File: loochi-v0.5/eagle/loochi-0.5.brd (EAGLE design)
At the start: 67.8 x 63.5 mm, 49 parts, among them IC1 ATTINY61M, J1 SPI_PRG, J2 POWER_JACKSMD, Q1 PMN25ENSOT457, Q2 PMN25ENSOT457, Q3 PMN25ENSOT457, Q4 FDC654P, U1 LZ4-00MC00BIGPADS, U2 APDS-9007, X1 SMA-SMD

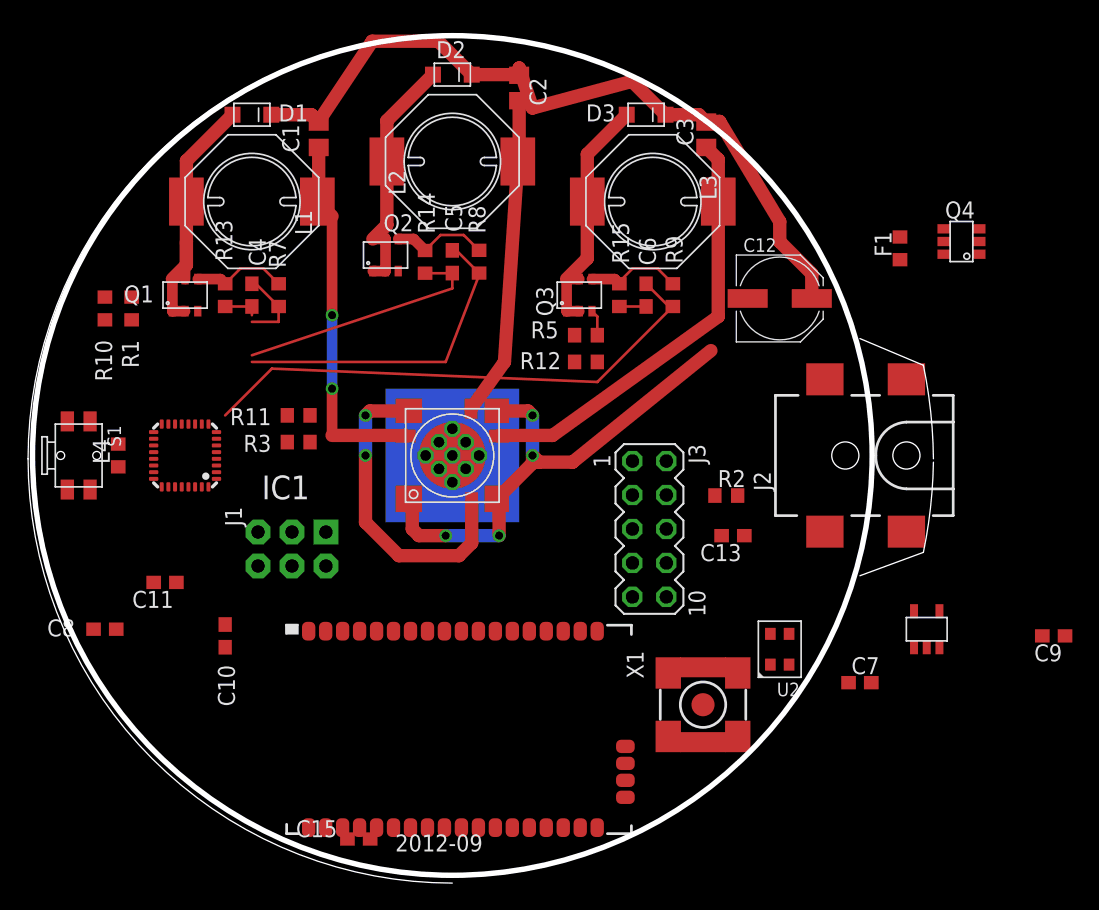
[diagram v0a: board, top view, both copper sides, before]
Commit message: Finalized board layout but have not run DRC yet.
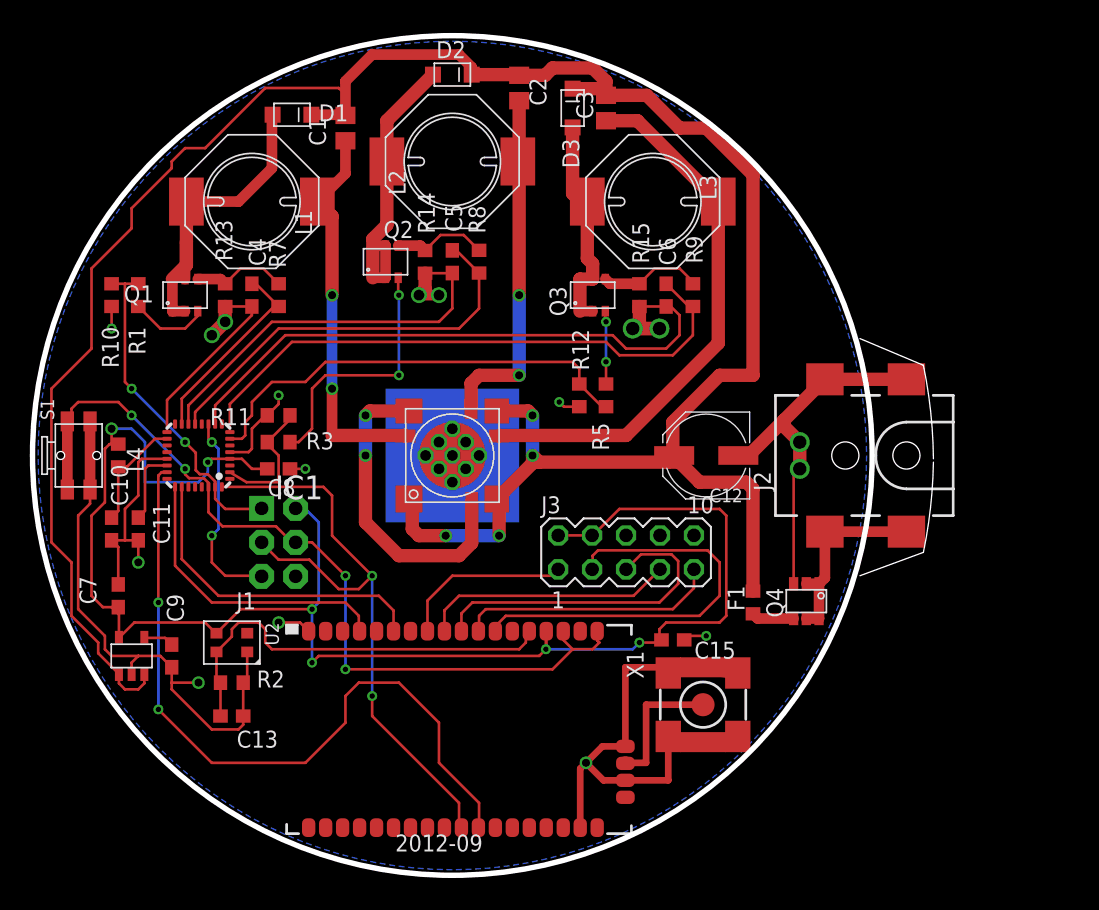
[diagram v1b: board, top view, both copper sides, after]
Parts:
- moved C9 66.0 mm to (11.0, 17.0), turned to 270 degrees
- moved U$1 59.5 mm to (8.00, 17.0)
- moved C7 55.9 mm to (7.00, 21.5), turned to 90 degrees
- moved U2 41.0 mm to (15.5, 18.0), turned to 180 degrees
- moved C13 39.9 mm to (15.5, 12.5), turned to 0 degrees
- moved R2 39.6 mm to (15.5, 15.0), turned to 180 degrees
- moved Q4 29.3 mm to (58.5, 21.1), turned to 180 degrees
- moved F1 28.7 mm to (54.5, 21.0)
- moved C15 27.8 mm to (48.5, 18.2), turned to 180 degrees
- moved C8 17.7 mm to (19.0, 31.0)
- moved C12 13.0 mm to (51.0, 32.0), turned to 180 degrees
- moved C10 11.7 mm to (6.50, 26.5)
- moved C3 7.76 mm to (43.5, 58.0)
- moved D3 5.52 mm to (41.0, 58.0), turned to 90 degrees
- moved R5 4.74 mm to (43.5, 36.5), turned to 90 degrees
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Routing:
- net GND: track 23.7 -> 248.0 mm, vias 0 -> 17
- net VCC: track 0.00 -> 120.7 mm, vias 0 -> 6
- net V+: track 96.4 -> 182.1 mm
- net BUTTON/MOSI: track 0.00 -> 63.3 mm, vias 0 -> 4
- net BLE-SCK: track 0.00 -> 54.9 mm, vias 0 -> 2
- net BLE-CS/SCK: track 0.00 -> 47.5 mm, vias 0 -> 2
- net BPWM: track 0.00 -> 33.8 mm
- net AIO0: track 0.00 -> 31.9 mm
- net N$15: track 0.00 -> 31.7 mm
- net RPWM/MISO: track 0.00 -> 25.1 mm, vias 0 -> 2
- net RSTB: track 0.00 -> 24.7 mm
- net BLE-MOSI: track 0.00 -> 24.4 mm
- net BLE-MISO: track 0.00 -> 22.4 mm
- net SPI_MISO: track 0.00 -> 19.5 mm
- net N$4: track 0.00 -> 19.3 mm, vias 0 -> 2
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- added copper zone on layer 16, net GND
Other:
- board size 67.8 x 63.5 mm -> 67.4 x 62.8 mm
- board text removed: "CC-BY-SA"
- board text removed: "Open-Source Hardware"

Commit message: Continued work on board v0.5 - Integrated Jurgen v0.5.1 changes - Shielded bsense - Holes for lenses - drc ok now
Next steps: BOM & check parts footprint
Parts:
- removed F1: MPZ2012, rcl:R0603
- removed J3: (no value), con-lstb:MA05-2
- added BLUE: (no value), WCI:CHIPLED_0603
- added C14, C16: 100n, rcl:C0603
- added C19: 0.1uF, rcl:C0603K
- added F2: MPZ2012, rcl:R0603
- added P1: 53047-0610, con-molex-picoblade:53047-0610
- added R18: 2, rcl:R0603
- added R4: 1k, rcl:R0603
- C7: value 10uF X5R Low ESR -> 10u
- Q4: value FDC654P -> SI7617DN; device mosfet:SUPERSOT6 -> Oma:POWERPAK1212-8
- moved C15 8.81 mm to (40.0, 20.5)
- moved X1 3.39 mm to (53.1, 15.8), turned to 135 degrees
- moved Q4 3.13 mm to (56.0, 23.0), turned to 0 degrees
- moved C7 1.12 mm to (6.50, 22.5)
- moved C13 0.50 mm to (15.5, 13.0)
- moved C8 0.50 mm to (19.0, 31.5)
- moved L4 0.50 mm to (7.50, 32.0)
- moved R11 0.50 mm to (19.0, 34.5)
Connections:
- removed net N$6: F1.1, Q4.P$4
- removed net RSTB: J3.5, U$2.CSB
- new net N$12: BLUE.C, R4.2
- new net N$16: R4.1, U$2.LED(1)
- new net N$21: C12.+, R18.1
- new net N$22: C19.2, F2.2, U$1.1, U$1.3
- new net SPI_CSB: P1.3, U$2.CSB
- new net SPI_RESET: P1.1, U$2.RESET
- net GND: now also C16.2, C19.1, P1.6, Q4.P$4; no longer J3.10, J3.6, J3.8, Q4.P$3
- net N$10: now also Q4.P$7, Q4.P$8; no longer Q4.P$1, Q4.P$2
- net N$15: now also C14.2, C16.1, X1.1; no longer J3.3, U$2.RESET
- net N$2: now also C14.1; no longer X1.1
- net SPI_CLK: now also P1.4; no longer J3.7
- net SPI_MISO: now also P1.5; no longer J3.9
- net SPI_MOSI: now also P1.2; no longer J3.1
- net V+: now also F2.1, Q4.P$1, Q4.P$2, Q4.P$3, R18.2; no longer C12.+, F1.2, U$1.1, U$1.3
- net VCC: now also BLUE.A; no longer J3.2, J3.4
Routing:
- net GND: track 248.0 -> 316.8 mm, vias 17 -> 18
- net VCC: track 120.7 -> 90.6 mm, vias 6 -> 4
- net N$16: track 0.00 -> 26.0 mm
- net RSTB: track 24.7 -> 0.00 mm
- net N$15: track 31.7 -> 9.29 mm
- net SPI_CSB: track 0.00 -> 20.2 mm
- net SPI_RESET: track 0.00 -> 19.9 mm
- net V+: track 182.1 -> 162.7 mm
- net N$22: track 0.00 -> 16.4 mm
- net SPI_MOSI: track 13.0 -> 25.7 mm
- net BLE-SCK: track 54.9 -> 42.9 mm
- net N$2: track 10.2 -> 3.65 mm
- net N$21: track 0.00 -> 5.28 mm
- net SPI_MISO: track 19.5 -> 15.2 mm, vias 0 -> 1
- net N$10: track 14.7 -> 11.5 mm
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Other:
- board size 67.4 x 62.8 mm -> 67.8 x 63.5 mm

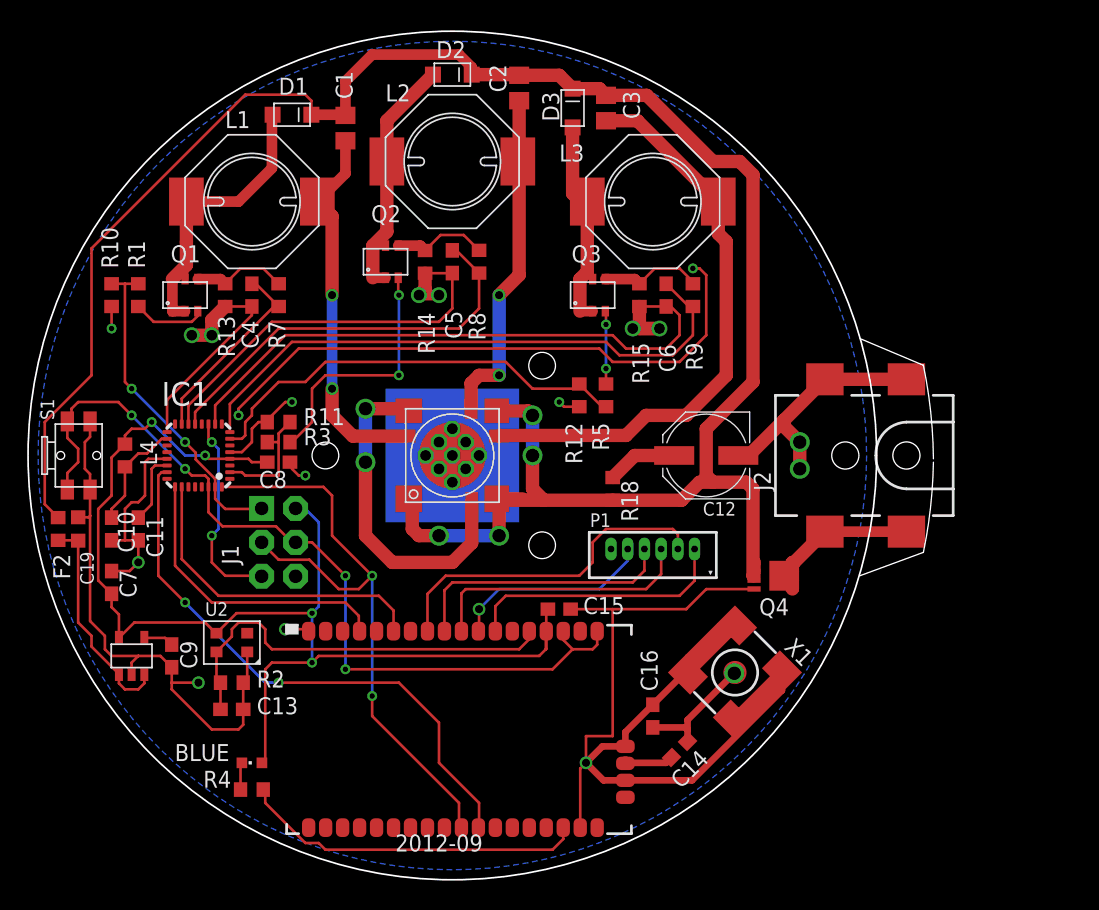
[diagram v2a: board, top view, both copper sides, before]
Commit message: More work on the board - almost final (antenna trace needs rework)
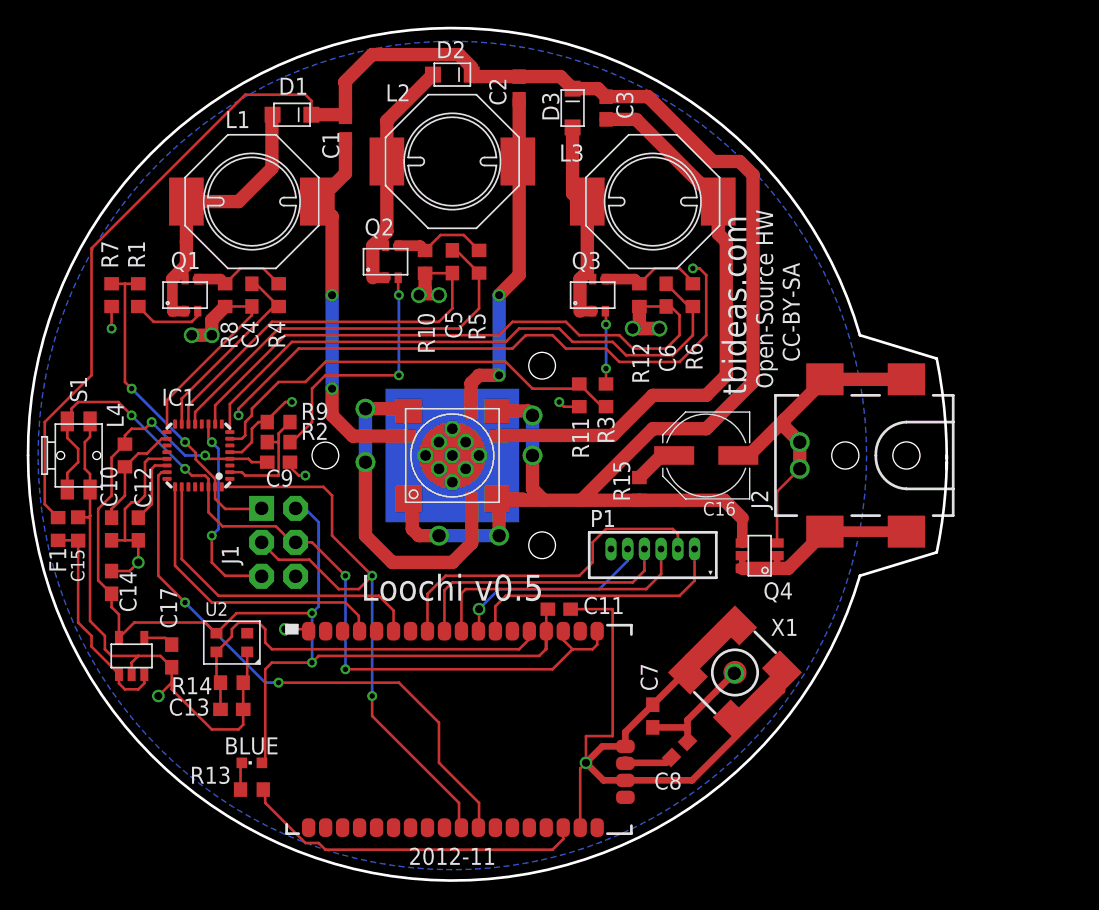
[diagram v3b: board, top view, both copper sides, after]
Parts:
- removed C19: 0.1uF, rcl:C0603K
- removed R18: 2, rcl:R0603
- added C17: 10nF, rcl:C0603
- added R6: 10k, rcl:R0603
- C1, C2, C3: device rcl:C0805 -> rcl:C0603
- C11, C8: value 0.1uF -> 100n
- C12: value 100uF -> 0.1uF; device rcl:PANASONIC_D -> rcl:C0603
- C14: value 100n -> 10u
- C15: value 100n -> 0.1uF; device rcl:C0603 -> rcl:C0603K
- C16: value 100n -> 100uF; device rcl:C0603 -> rcl:PANASONIC_D
- C7: value 10u -> 100n
- C9: value 10nF -> 0.1uF
- Q4: value SI7617DN -> (none); device Oma:POWERPAK1212-8 -> mosfet:SUPERSOT6
- R10, R12, R8: value 10k -> 0.1
- R13: value 0.1 -> 1k
- R14: value 0.1 -> 27k
- R15: value 0.1 -> 2
- R2: value 27k -> 10
- R4: value 1k -> 10k
- R5: value 10 -> 10k
- U$1: value LP2985 -> AIRCABLEBLPEXTANT; device ti-regulators:DBV -> aircable:AIRCABLEBLP
- U$2: value AIRCABLEBLPEXTANT -> LP2985; device aircable:AIRCABLEBLP -> ti-regulators:DBV
- moved C14 44.3 mm to (6.50, 22.5), turned to 90 degrees
- moved C12 42.9 mm to (8.50, 26.5), turned to 90 degrees
- moved C7 41.7 mm to (47.0, 12.5)
- moved R13 37.1 mm to (17.0, 7.00), turned to 180 degrees
- moved R4 37.1 mm to (19.0, 44.0), turned to 90 degrees
- moved C8 36.9 mm to (49.0, 10.0), turned to 45 degrees
- moved C15 36.5 mm to (4.00, 26.5), turned to 270 degrees
- moved R14 34.7 mm to (15.5, 15.0), turned to 180 degrees
- moved R9 32.4 mm to (19.0, 34.5), turned to 0 degrees
- moved C11 32.1 mm to (40.0, 20.5), turned to 180 degrees
- moved U$1 25.1 mm to (32.5, 11.5)
- moved U$2 25.1 mm to (8.00, 17.0)
- moved R3 24.7 mm to (43.5, 36.5), turned to 90 degrees
- moved R10 23.6 mm to (30.0, 46.5)
- moved R11 22.6 mm to (41.5, 36.5), turned to 90 degrees
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- renumbered F2 to F1
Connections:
- net AIO0: now also R14.2, U$1.AIO(0); no longer R2.2, U$2.AIO(0)
- net BLE-CS/SCK: now also U$1.PIO(4); no longer U$2.PIO(4)
- net BLE-MISO: now also U$1.RX; no longer U$2.RX
- net BLE-MOSI: now also U$1.TX; no longer U$2.TX
- net BLE-SCK: now also U$1.PIO(3); no longer U$2.PIO(3)
- net BPWM: now also R11.2, R3.1; no longer R12.2, R5.1
- net BSENSE: now also R6.1; no longer R9.1
- net BUTTON/MOSI: now also U$1.PIO(10), U$1.VREG_EN; no longer U$2.PIO(10), U$2.VREG_EN
- net GND: now also C12.1, C14.2, C16.-, C17.2, C9.1, Q4.P$3, R7.1, R8.1, R9.1, U$1.GND4, U$1.GND5, U$1.GND@28, U$1.GND@58, U$2.2; no longer C12.-, C16.2, C19.1, C8.1, C9.2, Q4.P$4, R13.1, R15.1, R2.1, U$1.2, U$2.GND4, U$2.GND5, U$2.GND@28, U$2.GND@58
- net GPWM: now also R2.1, R9.2; no longer R11.2, R3.1
- net GSENSE: now also R5.1; no longer R8.1
- net N$10: now also Q4.P$1, Q4.P$2; no longer Q4.P$7, Q4.P$8
- net N$12: now also R13.2; no longer R4.2
- net N$13: now also C17.1, U$2.4; no longer C9.1, U$1.4
- net N$15: now also C7.1, C8.2; no longer C14.2, C16.1
- net N$16: now also R13.1, U$1.LED(1); no longer R4.1, U$2.LED(1)
- net N$17: now also R10.2, R5.2; no longer R14.2, R8.2
- net N$2: now also C8.1, U$1.ANT; no longer C14.1, U$2.ANT
- net N$21: now also C16.+, R15.1; no longer C12.+, R18.1
- net N$22: now also C15.2, U$2.1, U$2.3; no longer C19.2, U$1.1, U$1.3
- net N$25: now also R12.2, R6.2; no longer R15.2, R9.2
- net N$3: now also R3.2; no longer R5.2
- net N$4: now also R2.2; no longer R3.2
- net N$7: now also R4.2, R8.2; no longer R13.2, R7.2
- net N$9: now also C12.2; no longer C11.2
- net RPWM/MISO: now also R7.2; no longer R10.2
- net RSENSE: now also R4.1; no longer R7.1
- net SPI_CLK: now also U$1.CLK; no longer U$2.CLK
- net SPI_CSB: now also U$1.CSB; no longer U$2.CSB
- net SPI_MISO: now also U$1.MISO; no longer U$2.MISO
- net SPI_MOSI: now also U$1.MOSI; no longer U$2.MOSI
- net SPI_RESET: now also U$1.RESET; no longer U$2.RESET
- net V+: now also Q4.P$4, R15.2; no longer Q4.P$1, Q4.P$2, Q4.P$3, R18.2
- net VCC: now also C11.2, C14.1, C9.2, U$1.VBATT, U$2.5; no longer C15.2, C7.1, C8.2, U$1.5, U$2.VBATT
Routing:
- net GND: track 316.8 -> 312.9 mm
- net N$10: track 11.5 -> 15.3 mm
- net N$21: track 5.28 -> 3.28 mm
- net V+: track 162.7 -> 161.3 mm
- net BSENSE: track 44.6 -> 45.4 mm
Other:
- board size 67.8 x 63.5 mm -> 68.8 x 63.8 mm
- board text added: "2012-11"
- board text added: "CC-BY-SA"
- board text added: "Loochi v0.5"
- board text added: "Open-Source HW"
- board text added: "tbideas.com"
- board text removed: "2012-09"
